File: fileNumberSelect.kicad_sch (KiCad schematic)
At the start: 13 parts

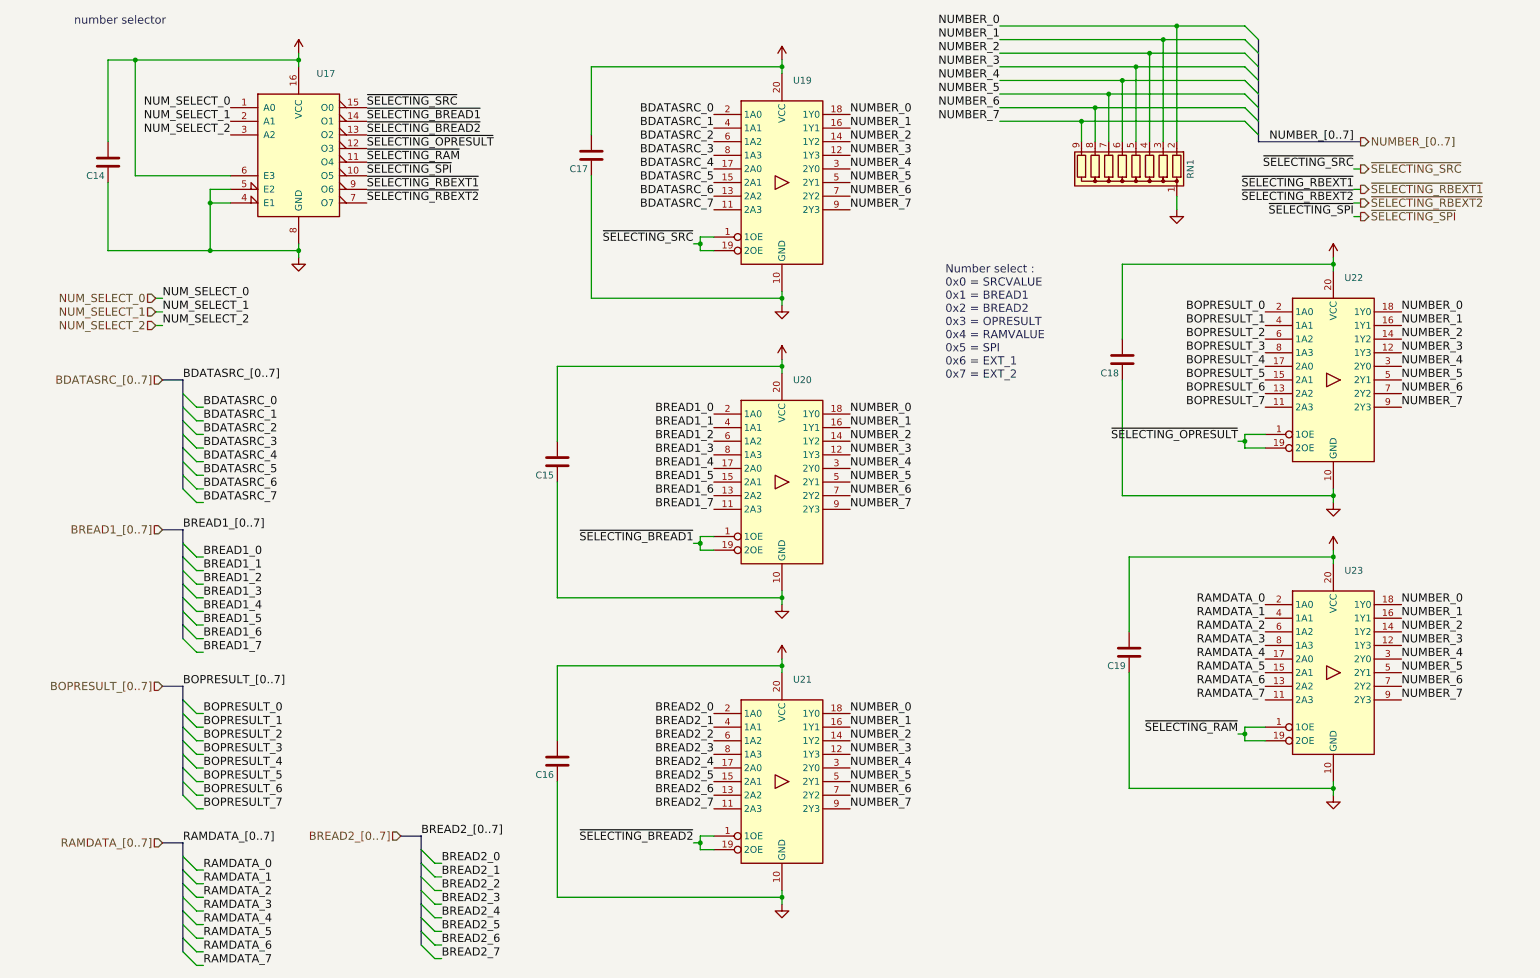
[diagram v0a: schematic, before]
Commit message: Updating descriptions
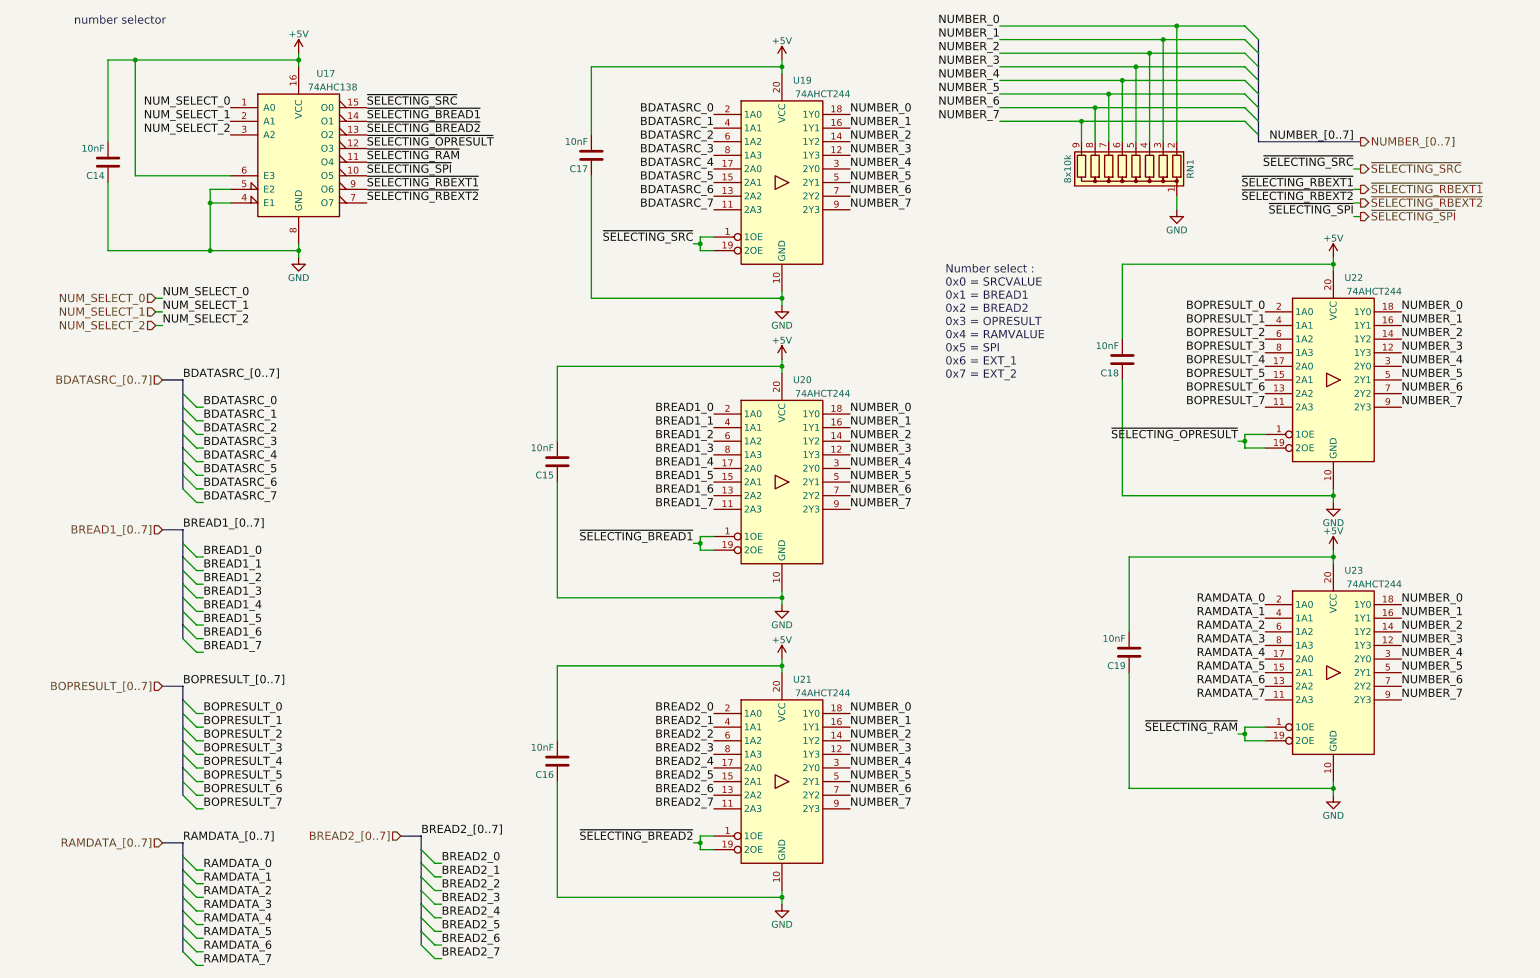
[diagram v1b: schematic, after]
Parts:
- C14, C15, C16, C17, C18, C19: value (none) -> 10nF; footprint (none) -> Capacitor_SMD:C_0805_2012Metric
- RN1: value (none) -> 8x10k; footprint (none) -> Resistor_THT:R_Array_SIP9
- U17: value (none) -> 74AHC138; footprint (none) -> Package_SO:SOIC-16W_5.3x10.2mm_P1.27mm
- U19, U20, U21, U22, U23: value (none) -> 74AHCT244; footprint (none) -> Package_SO:SOIC-20W_7.5x12.8mm_P1.27mm

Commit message: Renaming COUNTER to SEQUENCE and others to make it clear
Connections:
- net NUM_SELECT_0 renamed NUM_SELECT_BUF_0
- net NUM_SELECT_1 renamed NUM_SELECT_BUF_1
- net NUM_SELECT_2 renamed NUM_SELECT_BUF_2
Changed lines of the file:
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@@
     (effects (font (size 1.524 1.524)) (justify right bottom))
   )
-  (label "NUM_SELECT_1" (at 49.53 35.56 180)
+  (label "NUM_SELECT_BUF_1" (at 49.53 35.56 180)
     (effects (font (size 1.524 1.524)) (justify right bottom))
   )
@@
     (effects (font (size 1.524 1.524)) (justify left bottom))
   )
-  (label "NUM_SELECT_1" (at 36.83 71.12 0)
+  (label "NUM_SELECT_BUF_1" (at 36.83 71.12 0)
     (effects (font (size 1.524 1.524)) (justify left bottom))
   )
@@
     (effects (font (size 1.524 1.524)) (justify left bottom))
   )
-  (label "NUM_SELECT_2" (at 49.53 38.1 180)
+  (label "NUM_SELECT_BUF_2" (at 49.53 38.1 180)
     (effects (font (size 1.524 1.524)) (justify right bottom))
   )
@@
     (effects (font (size 1.524 1.524)) (justify right bottom))
   )
-  (label "NUM_SELECT_0" (at 49.53 33.02 180)
+  (label "NUM_SELECT_BUF_0" (at 49.53 33.02 180)
     (effects (font (size 1.524 1.524)) (justify right bottom))
   )
@@
     (effects (font (size 1.524 1.524)) (justify right bottom))
   )
-  (label "NUM_SELECT_0" (at 36.83 68.58 0)
+  (label "NUM_SELECT_BUF_0" (at 36.83 68.58 0)
     (effects (font (size 1.524 1.524)) (justify left bottom))
   )
@@
     (effects (font (size 1.524 1.524)) (justify left bottom))
   )
-  (label "NUM_SELECT_2" (at 36.83 73.66 0)
+  (label "NUM_SELECT_BUF_2" (at 36.83 73.66 0)
     (effects (font (size 1.524 1.524)) (justify left bottom))
   )
@@
     (effects (font (size 1.524 1.524)) (justify left))
   )
-  (hierarchical_label "NUM_SELECT_1" (shape input) (at 35.56 71.12 180)
+  (hierarchical_label "NUM_SELECT_BUF_1" (shape input) (at 35.56 71.12 180)
     (effects (font (size 1.524 1.524)) (justify right))
   )
@@
     (effects (font (size 1.524 1.524)) (justify right))
   )
-  (hierarchical_label "NUM_SELECT_2" (shape input) (at 35.56 73.66 180)
+  (hierarchical_label "NUM_SELECT_BUF_2" (shape input) (at 35.56 73.66 180)
     (effects (font (size 1.524 1.524)) (justify right))
   )
@@
     (effects (font (size 1.524 1.524)) (justify left))
   )
-  (hierarchical_label "NUM_SELECT_0" (shape input) (at 35.56 68.58 180)
-    (effects (font (size 1.524 1.524)) (justify right))
-  )
+  (hierarchical_label "NUM_SELECT_BUF_0" (shape input) (at 35.56 68.58 180)
+    (effects (font (size 1.524 1.524)) (justify right))
+  )

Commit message: bit of cleaning after last commit
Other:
- moved on the sheet: C14
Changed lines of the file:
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@@
   (junction (at 62.23 24.13) (diameter 0) (color 0 0 0 0)
   )
+  (junction (at 26.67 45.72) (diameter 0) (color 0 0 0 0)
+  )
   (junction (at 238.76 149.86) (diameter 0) (color 0 0 0 0)
   )
@@
   (junction (at 220.98 22.86) (diameter 0) (color 0 0 0 0)
   )
-  (junction (at 31.75 24.13) (diameter 0) (color 0 0 0 0)
-  )
   (junction (at 218.44 25.4) (diameter 0) (color 0 0 0 0)
   )
@@
     (stroke (width 0) (type default) (color 0 0 0 0))
   )
-  (wire (pts (xy 31.75 24.13) (xy 31.75 45.72))
-    (stroke (width 0) (type default) (color 0 0 0 0))
-  )
   (wire (pts (xy 137.16 171.45) (xy 139.7 171.45))
     (stroke (width 0) (type default) (color 0 0 0 0))
@@
     (stroke (width 0) (type default) (color 0 0 0 0))
   )
-  (wire (pts (xy 31.75 24.13) (xy 26.67 24.13))
+  (wire (pts (xy 26.67 24.13) (xy 62.23 24.13))
     (stroke (width 0) (type default) (color 0 0 0 0))
   )
@@
     (stroke (width 0) (type default) (color 0 0 0 0))
   )
-  (wire (pts (xy 26.67 46.99) (xy 26.67 59.69))
+  (wire (pts (xy 26.67 54.61) (xy 26.67 59.69))
     (stroke (width 0) (type default) (color 0 0 0 0))
   )
@@
     (stroke (width 0) (type default) (color 0 0 0 0))
   )
-  (wire (pts (xy 26.67 24.13) (xy 26.67 39.37))
+  (wire (pts (xy 26.67 24.13) (xy 26.67 45.72))
     (stroke (width 0) (type default) (color 0 0 0 0))
   )
@@
     (stroke (width 0) (type default) (color 0 0 0 0))
   )
+  (wire (pts (xy 26.67 45.72) (xy 26.67 46.99))
+    (stroke (width 0) (type default) (color 0 0 0 0))
+  )
   (wire (pts (xy 43.18 151.13) (xy 44.45 151.13))
     (stroke (width 0) (type default) (color 0 0 0 0))
@@
     (stroke (width 0) (type default) (color 0 0 0 0))
   )
-  (wire (pts (xy 62.23 24.13) (xy 31.75 24.13))
-    (stroke (width 0) (type default) (color 0 0 0 0))
-  )
-  (wire (pts (xy 49.53 45.72) (xy 31.75 45.72))
+  (wire (pts (xy 26.67 45.72) (xy 49.53 45.72))
     (stroke (width 0) (type default) (color 0 0 0 0))
   )
@@
     (pin "1")
   )
-  (symbol (lib_id "Device:C") (at 26.67 43.18 180) (unit 1)
+  (symbol (lib_id "Device:C") (at 26.67 50.8 180) (unit 1)
     (in_bom yes) (on_board yes)
-    (property "Reference" "C14" (id 0) (at 26.035 45.72 0)
+    (property "Reference" "C14" (id 0) (at 26.035 53.34 0)
       (effects (font (size 1.27 1.27)) (justify left))
     )
-    (property "Value" "10nF" (id 1) (at 26.035 40.64 0)
+    (property "Value" "10nF" (id 1) (at 26.035 48.26 0)
       (effects (font (size 1.27 1.27)) (justify left))
     )
-    (property "Footprint" "Capacitor_SMD:C_0805_2012Metric" (id 2) (at 25.7048 39.37 0)
+    (property "Footprint" "Capacitor_SMD:C_0805_2012Metric" (id 2) (at 25.7048 46.99 0)
       (effects (font (size 1.27 1.27)) hide)
     )
-    (property "Datasheet" "" (id 3) (at 26.67 43.18 0)
+    (property "Datasheet" "" (id 3) (at 26.67 50.8 0)
       (effects (font (size 1.27 1.27)) hide)
     )
